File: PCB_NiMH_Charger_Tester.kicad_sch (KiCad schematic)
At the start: 62 parts, among them J1 USB_C_Receptacle_PowerOnly_6P, J2 USB_C_Receptacle_USB2.0_16P, J3 UPDI Socket, J4 SSD1306, J5 Serial Header, Q1 DTC114EL, Q2 DTA114EL, Q3 MTB060P06I3, Q4 MTA100N10KRI3, SW1 SW_Push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

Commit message: Fix parts name
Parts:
- U2: value NJM7043 -> NJU7043
- U4: value TL431LP -> TL431
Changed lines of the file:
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@@
 			)
 		)
-		(property "Value" "NJM7043"
+		(property "Value" "NJU7043"
 			(at 143.51 113.03 0)
 			(effects
@@
 			)
 		)
-		(property "Value" "NJM7043"
+		(property "Value" "NJU7043"
 			(at 20.32 172.7199 0)
 			(effects
@@
 			)
 		)
-		(property "Value" "TL431LP"
+		(property "Value" "TL431"
 			(at 114.3 30.4799 90)
 			(effects
@@
 			)
 		)
-		(property "Value" "NJM7043"
+		(property "Value" "NJU7043"
 			(at 143.51 132.08 0)
 			(effects

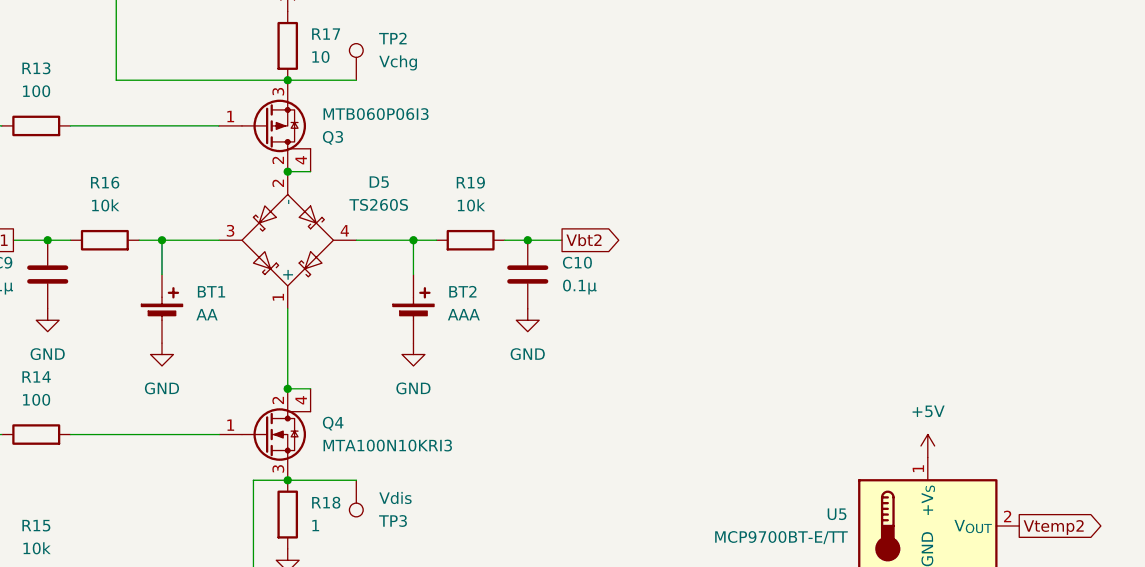
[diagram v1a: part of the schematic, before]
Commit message: Update
* Adjust the position of SS1306.
* Support S1ZB20.
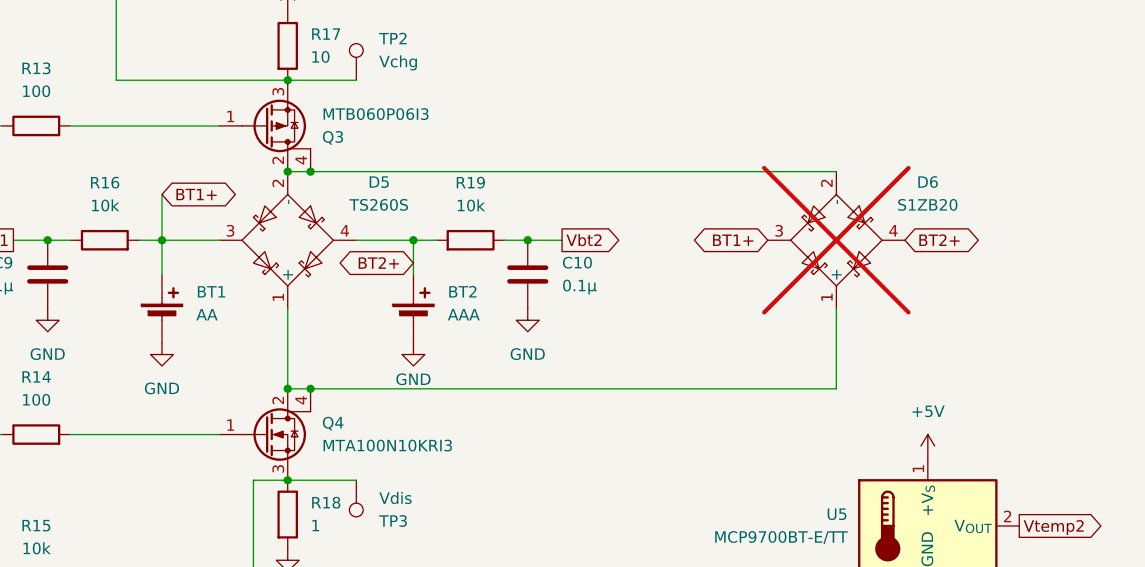
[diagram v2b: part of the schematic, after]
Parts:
- added D6: S1ZB20, Package_DIP:DIP-4_W7.62mm, symbol mylib:TS260S
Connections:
- net BT2+: now reaches BT2.1 (+), D5.4, R19.2
- net BT2+: now also D6.4
- net at D5.1 (+), Q4.2 (D), Q4.4 (D): now also D6.1 (+)
- net at D5.2 (-), Q3.2 (D), Q3.4 (D): now also D6.2 (-)
- net BT1+: now reaches BT1.1 (+), D5.3, R16.2
- net BT1+: now also D6.3
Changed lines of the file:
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@@
 	)
 	(junction
+		(at 186.69 110.49)
+		(diameter 0)
+		(color 0 0 0 0)
+	)
+	(junction
 		(at 184.15 144.78)
 		(diameter 0)
@@
 	)
 	(junction
+		(at 186.69 134.62)
+		(diameter 0)
+		(color 0 0 0 0)
+	)
+	(junction
 		(at 116.84 87.63)
 		(diameter 0)
@@
 	(wire
 		(pts
+			(xy 198.12 118.11) (xy 198.12 121.92)
+		)
+		(stroke
+			(width 0)
+			(type default)
+		)
+	)
+	(wire
+		(pts
 			(xy 116.84 156.21) (xy 116.84 171.45)
 		)
@@
 	(wire
 		(pts
+			(xy 245.11 125.73) (xy 245.11 134.62)
+		)
+		(stroke
+			(width 0)
+			(type default)
+		)
+	)
+	(wire
+		(pts
 			(xy 109.22 26.67) (xy 111.76 26.67)
 		)
@@
 	(wire
 		(pts
+			(xy 245.11 134.62) (xy 186.69 134.62)
+		)
+		(stroke
+			(width 0)
+			(type default)
+		)
+	)
+	(wire
+		(pts
 			(xy 135.89 156.21) (xy 135.89 151.13)
 		)
@@
 	(wire
 		(pts
-			(xy 184.15 110.49) (xy 186.69 110.49)
+			(xy 170.18 113.03) (xy 170.18 118.11)
 		)
 		(stroke
@@
 	(wire
 		(pts
-			(xy 69.85 119.38) (xy 78.74 119.38)
+			(xy 184.15 110.49) (xy 186.69 110.49)
 		)
 		(stroke
@@
 	(wire
 		(pts
-			(xy 121.92 137.16) (xy 135.89 137.16)
+			(xy 69.85 119.38) (xy 78.74 119.38)
 		)
 		(stroke
@@
 	(wire
 		(pts
-			(xy 46.99 69.85) (xy 46.99 38.1)
+			(xy 121.92 137.16) (xy 135.89 137.16)
 		)
 		(stroke
@@
 	(wire
 		(pts
-			(xy 80.01 21.59) (xy 80.01 25.4)
+			(xy 46.99 69.85) (xy 46.99 38.1)
 		)
 		(stroke
@@
 	(wire
 		(pts
-			(xy 49.53 106.68) (xy 52.07 106.68)
+			(xy 80.01 21.59) (xy 80.01 25.4)
 		)
 		(stroke
@@
 	(wire
 		(pts
-			(xy 198.12 118.11) (xy 198.12 121.92)
+			(xy 49.53 106.68) (xy 52.07 106.68)
 		)
 		(stroke
@@
 	(wire
 		(pts
+			(xy 186.69 110.49) (xy 245.11 110.49)
+		)
+		(stroke
+			(width 0)
+			(type default)
+		)
+	)
+	(wire
+		(pts
 			(xy 109.22 137.16) (xy 111.76 137.16)
 		)
@@
 		)
 	)
+	(global_label "BT1+"
+		(shape bidirectional)
+		(at 237.49 118.11 180)
+		(fields_autoplaced yes)
+		(effects
+			(font
+				(size 1.27 1.27)
+			)
+			(justify right)
+		)
+		(property "Intersheetrefs" "${INTERSHEET_REFS}"
+			(at 228.374 118.11 0)
+			(effects
+				(font
+					(size 1.27 1.27)
+				)
+				(justify right)
+				(hide yes)
+			)
+		)
+	)
 	(global_label "UPDI"
 		(shape bidirectional)
@@
 		)
 	)
+	(global_label "BT2+"
+		(shape bidirectional)
+		(at 198.12 120.65 180)
+		(fields_autoplaced yes)
+		(effects
+			(font
+				(size 1.27 1.27)
+			)
+			(justify right)
+		)
+		(property "Intersheetrefs" "${INTERSHEET_REFS}"
+			(at 189.004 120.65 0)
+			(effects
+				(font
+					(size 1.27 1.27)
+				)
+				(justify right)
+				(hide yes)
+			)
+		)
+	)
 	(global_label "ChgCtl"
 		(shape output)
@@
 		)
 	)
+	(global_label "BT1+"
+		(shape bidirectional)
+		(at 170.18 113.03 0)
+		(fields_autoplaced yes)
+		(effects
+			(font
+				(size 1.27 1.27)
+			)
+			(justify left)
+		)
+		(property "Intersheetrefs" "${INTERSHEET_REFS}"
+			(at 179.296 113.03 0)
+			(effects
+				(font
+					(size 1.27 1.27)
+				)
+				(justify left)
+				(hide yes)
+			)
+		)
+	)
 	(global_label "Vbt2"
 		(shape output)
@@
 		)
 	)
+	(global_label "BT2+"
+		(shape bidirectional)
+		(at 252.73 118.11 0)
+		(fields_autoplaced yes)
+		(effects
+			(font
+				(size 1.27 1.27)
+			)
+			(justify left)
+		)
+		(property "Intersheetrefs" "${INTERSHEET_REFS}"
+			(at 261.846 118.11 0)
+			(effects
+				(font
+					(size 1.27 1.27)
+				)
+				(justify left)
+				(hide yes)
+			)
+		)
+	)
 	(global_label "Vbt2"
 		(shape input)
@@
 		(on_board yes)
 		(dnp no)
-		(fields_autoplaced yes)
 		(property "Reference" "#PWR035"
 			(at 198.12 135.89 0)
@@
 		)
 		(property "Value" "GND"
-			(at 198.12 134.62 0)
+			(at 198.12 133.604 0)
 			(effects
 				(font
@@
 					(unit 1)
 				)
+			)
+		)
+	)
+	(symbol
+		(lib_id "mylib:TS260S")
+		(at 245.11 118.11 270)
+		(unit 1)
+		(exclude_from_sim no)
+		(in_bom yes)
+		(on_board yes)
+		(dnp yes)
+		(fields_autoplaced yes)
+		(property "Reference" "D6"
+			(at 255.27 111.6898 90)
+			(effects
+				(font
+					(size 1.27 1.27)
+				)
+			)
+		)
+		(property "Value" "S1ZB20"
+			(at 255.27 114.2298 90)
+			(effects
+				(font
+					(size 1.27 1.27)
+				)
+			)
+		)
+		(property "Footprint" "Package_DIP:DIP-4_W7.62mm"
+			(at 245.11 118.11 0)
+			(effects
+				(font
+					(size 1.27 1.27)
+				)
+				(hide yes)
+			)
+		)
+		(property "Datasheet" "https://www.mouser.jp/datasheet/2/366/J534S1ZB-1203344.pdf"
+			(at 245.11 118.11 0)
+			(effects
+				(font
+					(size 1.27 1.27)
+				)
+				(hide yes)
+			)
+		)
+		(property "Description" "Schottky Bridge, 200V Vrms, 1A If, DIP-4"
+			(at 245.11 118.11 0)
+			(effects
+				(font
+					(size 1.27 1.27)
+				)
+				(hide yes)
+			)
+		)
+		(pin "4"
+		)
+		(pin "3"
+		)
+		(pin "1"
+		)
+		(pin "2"
+		)
+		(instances
+			(project "PCB_NiMH_Charger_Tester"
+				(path "/d20e9c0c-3c6f-4c5b-a7e9-4a9116696809"
+					(reference "D6")
+					(unit 1)
+				)

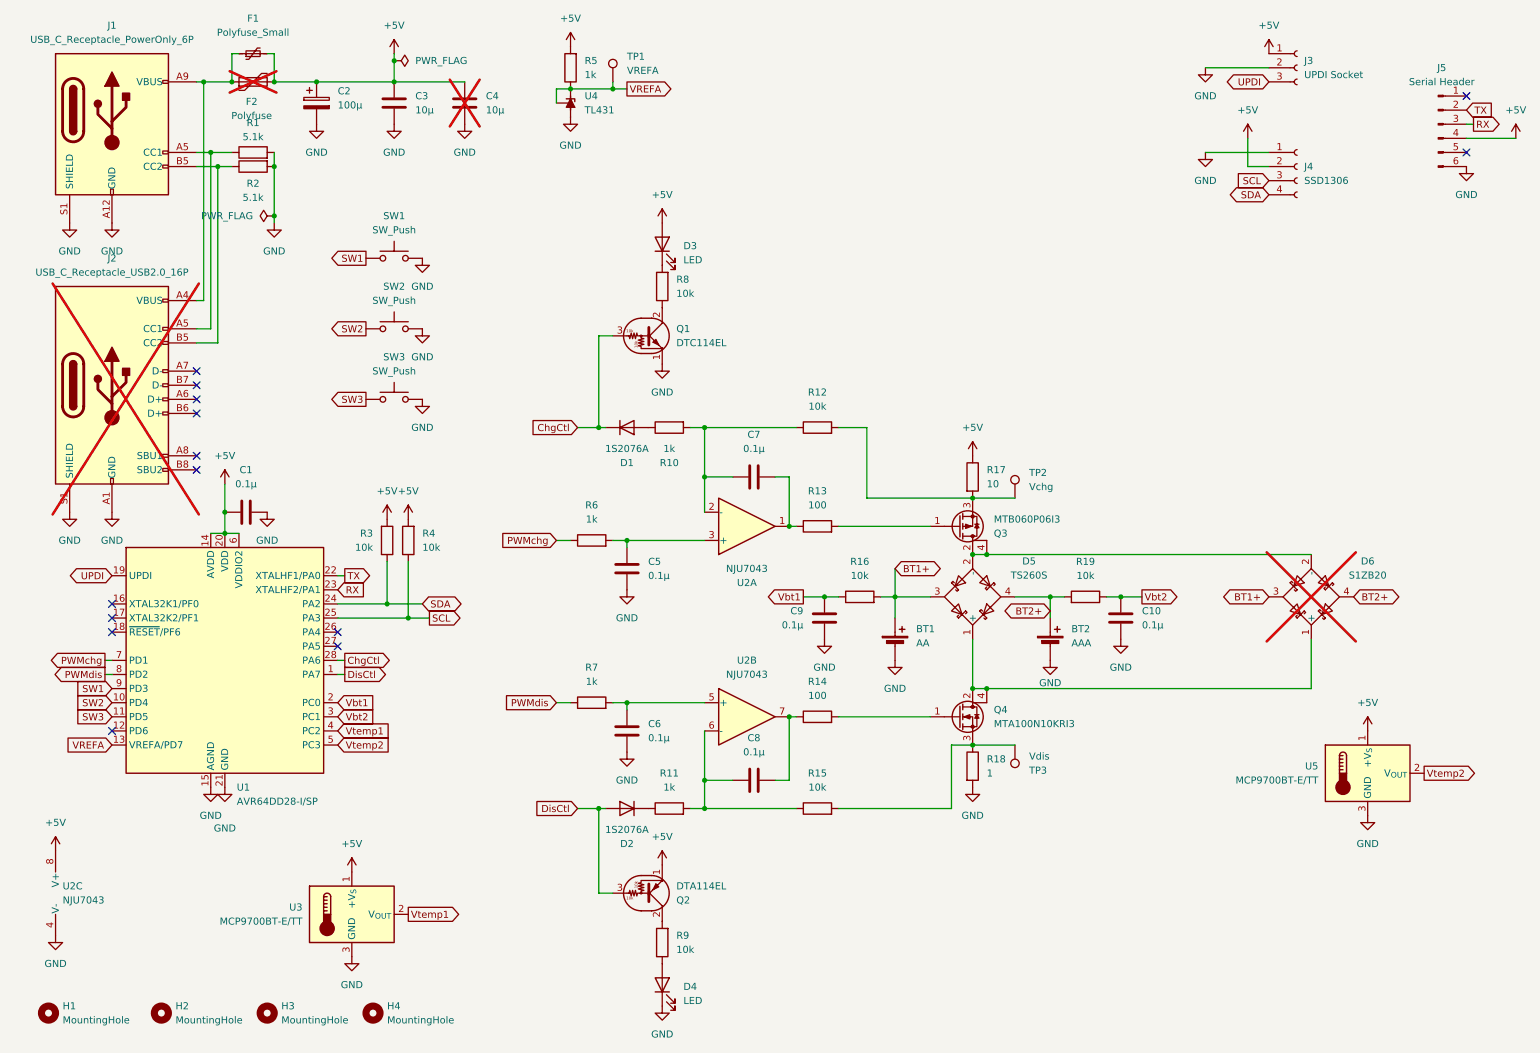
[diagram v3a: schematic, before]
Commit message: Update UPDI connector
Use the official UPDI v2 connector.

See "AVR Programming Adapter":
https://www.microchip.com/en-us/development-tool/AC31S18A
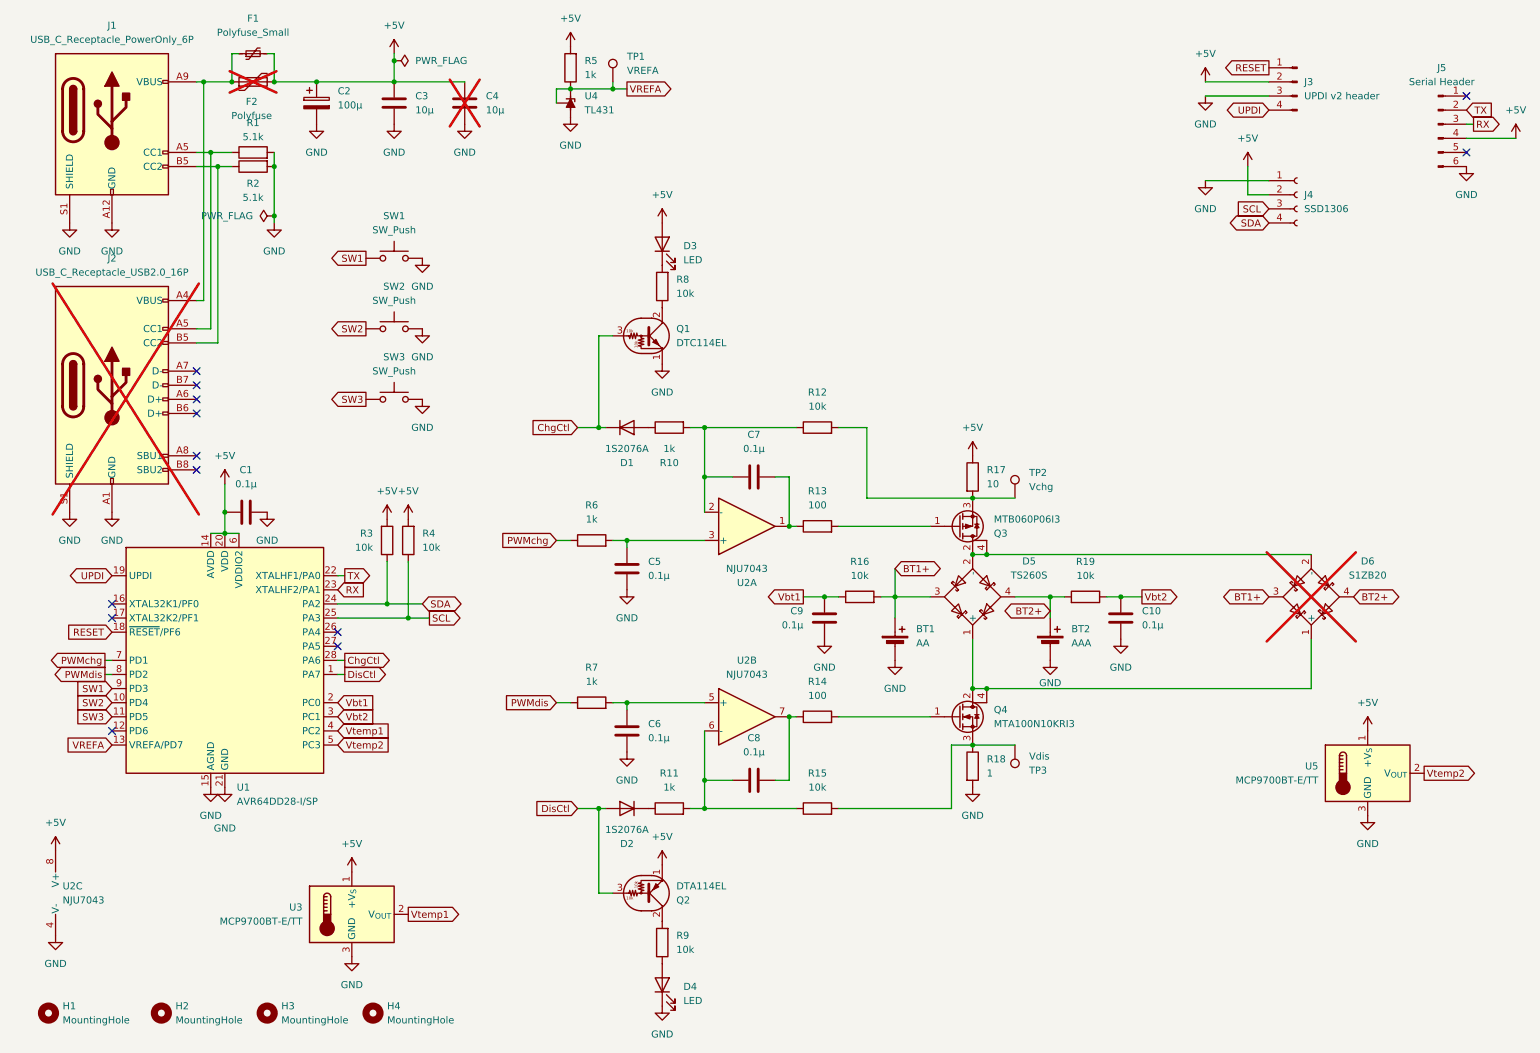
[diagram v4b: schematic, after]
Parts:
- removed J3: UPDI Socket, Connector_PinSocket_2.54mm:PinSocket_1x03_P2.54mm_Vertical, symbol Connector:Conn_01x03_Socket
- added J3: UPDI v2 header, Connector_PinHeader_2.54mm:PinHeader_1x04_P2.54mm_Vertical, symbol Connector:Conn_01x04_Pin
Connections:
- net +5V: now also J3.2 (Pin_2)
- net GND: now also J3.3 (Pin_3)
- net UPDI: now also J3.4 (Pin_4)
- net RESET: now reaches U1.18 (~{RESET}/PF6)
- net RESET: now also J3.1 (Pin_1)
- no-connect marks 14 -> 13
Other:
- moved on the sheet: J4

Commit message: Adjust resistor values
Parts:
- R10, R11: value 1k -> 4.7k
- R12, R15: value 10k -> 47k
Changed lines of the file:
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@@
 			)
 		)
-		(property "Value" "10k"
+		(property "Value" "47k"
 			(at 156.21 152.4 90)
 			(effects
@@
 			)
 		)
-		(property "Value" "1k"
+		(property "Value" "4.7k"
 			(at 129.54 91.44 90)
 			(effects
@@
 			)
 		)
-		(property "Value" "10k"
+		(property "Value" "47k"
 			(at 156.21 83.82 90)
 			(effects
@@
 			)
 		)
-		(property "Value" "1k"
+		(property "Value" "4.7k"
 			(at 129.54 152.4 90)
 			(effects

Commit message: Replace S1ZB20 symbol
It is not a Schottky Bridge, PN Bridge.
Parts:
- removed D6: S1ZB20, Package_DIP:DIP-4_W7.62mm, symbol mylib:TS260S
- added D6: S1ZB20, Package_DIP:DIP-4_W7.62mm, symbol Diode_Bridge:B40C800DM
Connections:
- net BT1+: now also D6.3
- net BT2+: now also D6.4
- net at D5.1 (+), Q4.2 (D), Q4.4 (D): now also D6.1 (+)
- net at D5.2 (-), Q3.2 (D), Q3.4 (D): now also D6.2 (-)
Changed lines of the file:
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@@
+	)
+	(symbol
+		(lib_id "Diode_Bridge:B40C800DM")
+		(at 245.11 118.11 270)
+		(unit 1)
+		(exclude_from_sim no)
+		(in_bom yes)
+		(on_board yes)
+		(dnp yes)
+		(fields_autoplaced yes)
+		(property "Reference" "D6"
+			(at 255.27 111.6898 90)
+			(effects
+				(font
+					(size 1.27 1.27)
+				)
+			)
+		)
+		(property "Value" "S1ZB20"
+			(at 255.27 114.2298 90)
+			(effects
+				(font
+					(size 1.27 1.27)
+				)
+			)
+		)
+		(property "Footprint" "Package_DIP:DIP-4_W7.62mm"
+			(at 248.285 121.92 0)
+			(effects
+				(font
+					(size 1.27 1.27)
+				)
+				(justify left)
+				(hide yes)
+			)
+		)
+		(property "Datasheet" "https://www.mouser.jp/datasheet/2/366/J534S1ZB-1203344.pdf"
+			(at 245.11 118.11 0)
+			(effects
+				(font
+					(size 1.27 1.27)
+				)
+				(hide yes)
+			)
+		)
+		(property "Description" "Diode Bridge, 200V Vrms, 1A If, DIP-4"
+			(at 245.11 118.11 0)
+			(effects
+				(font
+					(size 1.27 1.27)
+				)
+				(hide yes)
+			)
+		)
+		(pin "3"
+		)
+		(pin "1"
+		)
+		(pin "4"
+		)
+		(pin "2"
+		)
+		(instances
+			(project ""
+				(path "/d20e9c0c-3c6f-4c5b-a7e9-4a9116696809"
+					(reference "D6")
+					(unit 1)
+				)
+			)
+		)
 	)
 	(symbol
@@
 					(unit 1)
 				)
-			)
-		)
-	)
-	(symbol
-		(lib_id "mylib:TS260S")
-		(at 245.11 118.11 270)
-		(unit 1)
-		(exclude_from_sim no)
-		(in_bom yes)
-		(on_board yes)
-		(dnp yes)
-		(fields_autoplaced yes)
-		(property "Reference" "D6"
-			(at 255.27 111.6898 90)
-			(effects
-				(font
-					(size 1.27 1.27)
-				)
-			)
-		)
-		(property "Value" "S1ZB20"
-			(at 255.27 114.2298 90)
-			(effects
-				(font
-					(size 1.27 1.27)
-				)
-			)
-		)
-		(property "Footprint" "Package_DIP:DIP-4_W7.62mm"
-			(at 245.11 118.11 0)
-			(effects
-				(font
-					(size 1.27 1.27)
-				)
-				(hide yes)
-			)
-		)
-		(property "Datasheet" "https://www.mouser.jp/datasheet/2/366/J534S1ZB-1203344.pdf"
-			(at 245.11 118.11 0)
-			(effects
-				(font
-					(size 1.27 1.27)
-				)
-				(hide yes)
-			)
-		)
-		(property "Description" "Schottky Bridge, 200V Vrms, 1A If, DIP-4"
-			(at 245.11 118.11 0)
-			(effects
-				(font
-					(size 1.27 1.27)
-				)
-				(hide yes)
-			)
-		)
-		(pin "4"
-		)
-		(pin "3"
-		)
-		(pin "1"
-		)
-		(pin "2"
-		)
-		(instances
-			(project "PCB_NiMH_Charger_Tester"
-				(path "/d20e9c0c-3c6f-4c5b-a7e9-4a9116696809"
-					(reference "D6")
-					(unit 1)
-				)

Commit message: Reverse Serial Header
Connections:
- net +5V: now also J5.3 (Pin_3); no longer J5.4 (Pin_4)
- net GND: now also J5.1 (Pin_1); no longer J5.6 (Pin_6)
- net RX: now also J5.4 (Pin_4); no longer J5.3 (Pin_3)
- net TX: now also J5.5 (Pin_5); no longer J5.2 (Pin_2)
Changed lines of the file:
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@@
 	(title_block
 		(title "NiMH Charger & Tester")
-		(date "2025-08-25")
+		(date "2025-09-05")
 		(rev "2")
 		(company "K.Takata")
@@
 	(symbol
 		(lib_id "Connector:Conn_01x06_Pin")
-		(at 267.97 33.02 0)
+		(at 267.97 35.56 0)
+		(mirror x)
 		(unit 1)
 		(exclude_from_sim no)
@@
 		(on_board yes)
 		(dnp no)
-		(fields_autoplaced yes)
 		(property "Reference" "J5"
-			(at 268.605 22.86 0)
+			(at 268.478 23.876 0)
 			(effects
 				(font
@@
 		)
 		(property "Value" "Serial Header"
-			(at 268.605 25.4 0)
+			(at 268.478 21.336 0)
 			(effects
 				(font
@@
 		)
 		(property "Footprint" "Connector_PinHeader_2.54mm:PinHeader_1x06_P2.54mm_Vertical"
-			(at 267.97 33.02 0)
+			(at 267.97 35.56 0)
 			(effects
 				(font
@@
 		)
 		(property "Datasheet" "~"
-			(at 267.97 33.02 0)
+			(at 267.97 35.56 0)
 			(effects
 				(font
@@
 		)
 		(property "Description" "Generic connector, single row, 01x06, script generated"
-			(at 267.97 33.02 0)
+			(at 267.97 35.56 0)
 			(effects
 				(font
